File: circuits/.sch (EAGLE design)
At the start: 39 parts, among them U1 OPA344, U2 ATMEGA328P_TQFP, U3 ADMP401

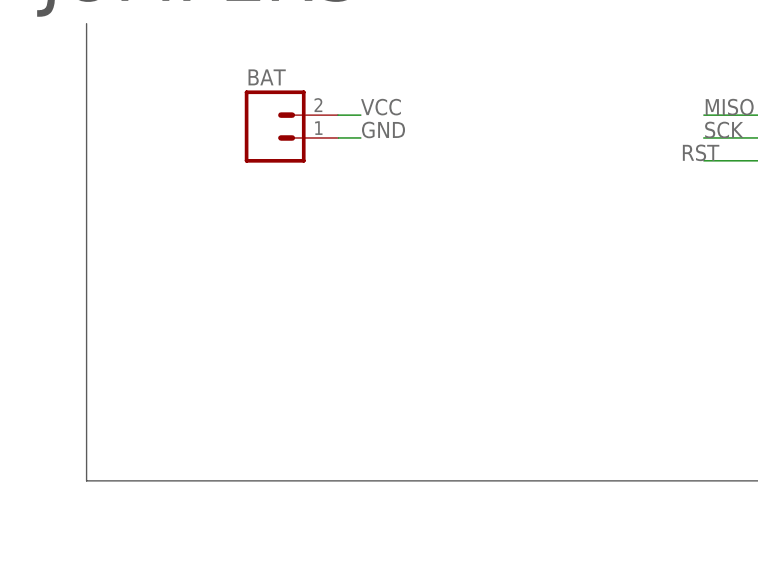
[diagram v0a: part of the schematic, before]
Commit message: parts csv and schematic without mic
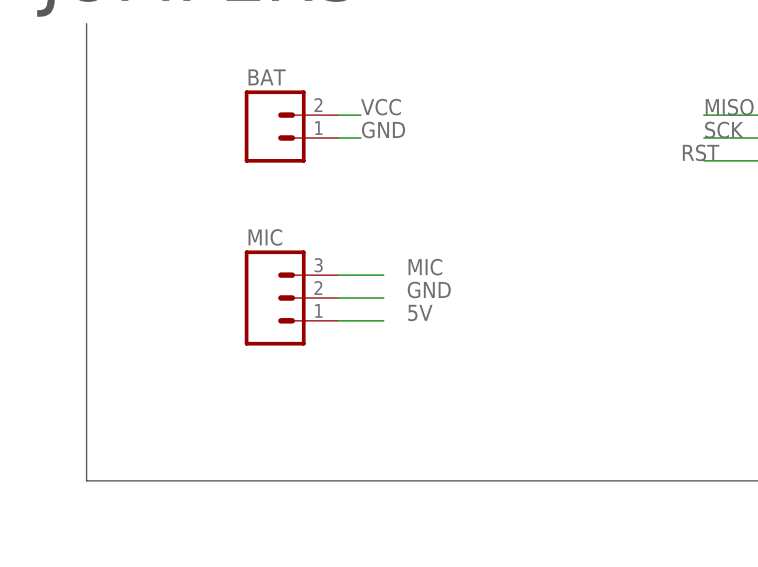
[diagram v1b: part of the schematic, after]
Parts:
- added MIC: (no value), SparkFun-Connectors:M03PTH
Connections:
- net 5V: now also MIC.1
- net GND: now also MIC.2
- net MIC: now also MIC.3
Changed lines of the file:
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@@
 <part name="NRFCAP" library="talkingdrums" deviceset="POLCAP-PANASONIC-SMD-C" device="" value="33uF"/>
 <part name="SC2" library="adafruit" deviceset="DIODE" device="_SOD-123FL"/>
+<part name="MIC" library="SparkFun-Connectors" deviceset="M03" device="PTH"/>
 </parts>
 <sheets>
@@
 <instance part="NRFCAP" gate="G$1" x="152.4" y="-269.24" rot="R180"/>
 <instance part="SC2" gate="G$1" x="137.16" y="-170.18"/>
+<instance part="MIC" gate="J$1" x="20.32" y="-259.08"/>
 </instances>
 <busses>
@@
 <label x="93.98" y="-497.84" size="1.778" layer="95"/>
 </segment>
+<segment>
+<pinref part="MIC" gate="J$1" pin="1"/>
+<wire x1="27.94" y1="-261.62" x2="33.02" y2="-261.62" width="0.1524" layer="91"/>
+<label x="35.56" y="-261.62" size="1.778" layer="95"/>
+</segment>
 </net>
 <net name="GND" class="0">
@@
 <wire x1="154.94" y1="-269.24" x2="165.1" y2="-269.24" width="0.1524" layer="91"/>
 <label x="167.64" y="-269.24" size="1.778" layer="95"/>
+</segment>
+<segment>
+<pinref part="MIC" gate="J$1" pin="2"/>
+<wire x1="27.94" y1="-259.08" x2="33.02" y2="-259.08" width="0.1524" layer="91"/>
+<label x="35.56" y="-259.08" size="1.778" layer="95"/>
 </segment>
 </net>
@@
 <label x="106.68" y="-342.9" size="1.778" layer="95"/>
 </segment>
-</net>
+<segment>
+<pinref part="MIC" gate="J$1" pin="3"/>
+<wire x1="27.94" y1="-256.54" x2="33.02" y2="-256.54" width="0.1524" layer="91"/>
+<label x="35.56" y="-256.54" size="1.778" layer="95"/>
+</segment>
+</net>
